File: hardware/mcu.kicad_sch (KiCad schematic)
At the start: 38 parts, among them J1 USB-C, SW3 RUN, SW4 BOOTSEL, SW5 WP, U20 RP2350B, U21 GD25Q128ESIGR, Y1 12MHz

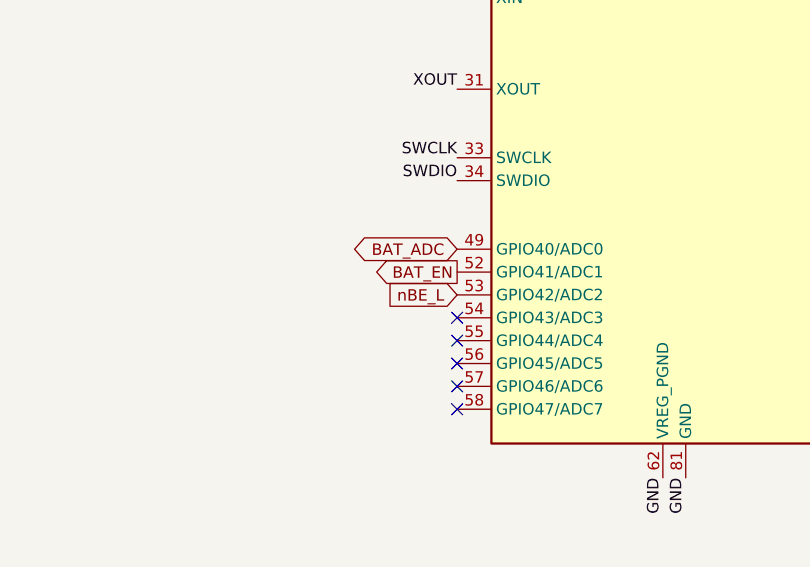
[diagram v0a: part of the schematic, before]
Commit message: Board: battery holder and switch checked against drawings; re-routed
Battery holder: Keystone 3034's footprint was wrong for the Q&J
CR2032-BS-6-1 (C70377), which has a + tab at one end and a - tab at the
other. New project footprint from Q&J's drawing QJ.BS-6: two 4.2 x 3.0 mm
pads, 26 mm apart inside, 32 mm outside. BT1 turned 90 degrees to fit.

Slide switch: KiCad's MSK12C02 footprint matches the drawing. SW5 moved
right 2.1 mm so the actuator tip sits at the board edge.

Re-routing then left nets from the RP2350B's top pad row open, so
preroute.py now fans pins 42-48 (PA16-PA20, WINH, nWP) into lanes to the
right. For room, C27 moved up and BAT_ADC moved from GPIO40 to GPIO43
(ADC3). Routed by flow.py on its second attempt, DRC clean at every
severity: 1765 track segments, 320 vias.

Co-Authored-By: Claude Opus 5.5 <noreply@anthropic.com>
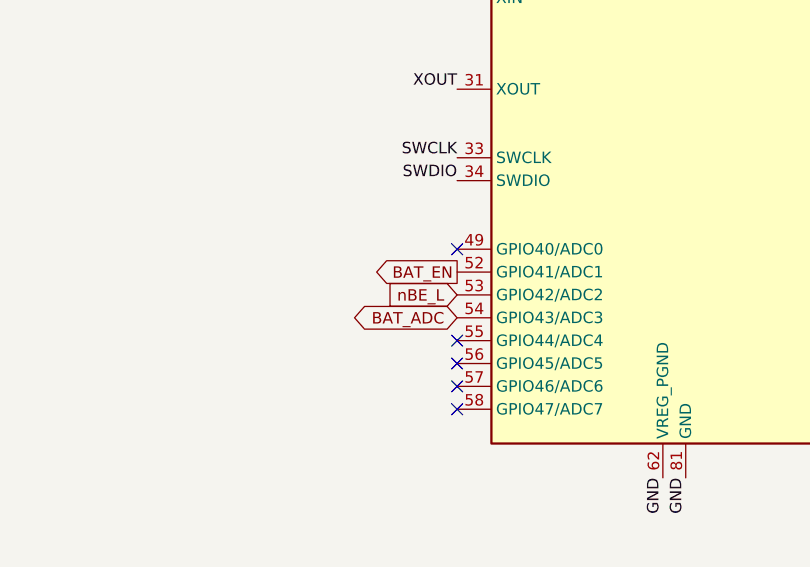
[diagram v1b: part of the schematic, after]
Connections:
- net BAT_ADC: now also U20.54 (GPIO43/ADC3); no longer U20.49 (GPIO40/ADC0)
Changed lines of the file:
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@@
   (global_label "WINH" (shape output) (at 154.94 198.12 0) (effects (font (size 1.27 1.27)) (justify left)))
   (global_label "nWP" (shape input) (at 154.94 200.66 0) (effects (font (size 1.27 1.27)) (justify left)))
-  (global_label "BAT_ADC" (shape bidirectional) (at 104.14 182.88 180) (effects (font (size 1.27 1.27)) (justify right)))
   (global_label "BAT_EN" (shape output) (at 104.14 185.42 180) (effects (font (size 1.27 1.27)) (justify right)))
   (global_label "nBE_L" (shape input) (at 104.14 187.96 180) (effects (font (size 1.27 1.27)) (justify right)))
-  (no_connect (at 104.14 190.50))
+  (global_label "BAT_ADC" (shape bidirectional) (at 104.14 190.50 180) (effects (font (size 1.27 1.27)) (justify right)))
+  (no_connect (at 104.14 182.88))
   (no_connect (at 104.14 193.04))
   (no_connect (at 104.14 195.58))
